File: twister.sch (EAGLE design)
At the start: 30 parts, among them IC1 A3967SLB, U2 ARDUINO_SHIELDNOHOLES

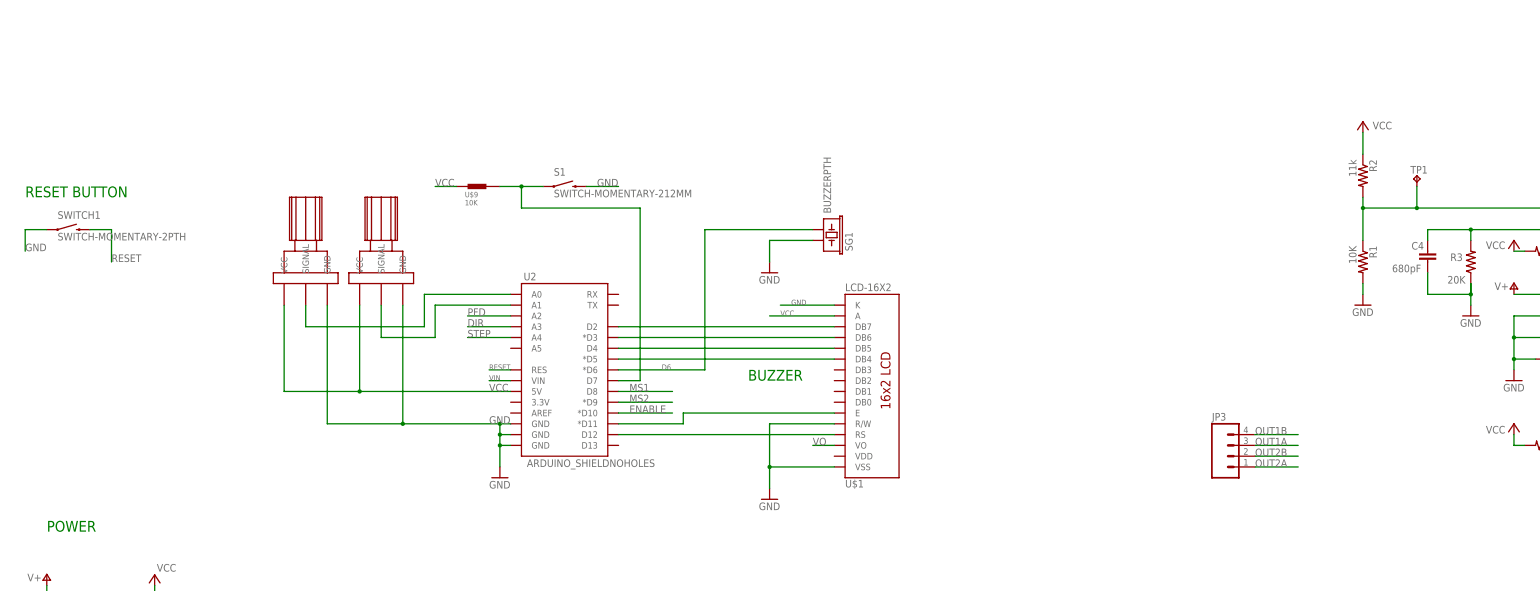
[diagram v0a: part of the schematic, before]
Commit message: Added stepper motor.
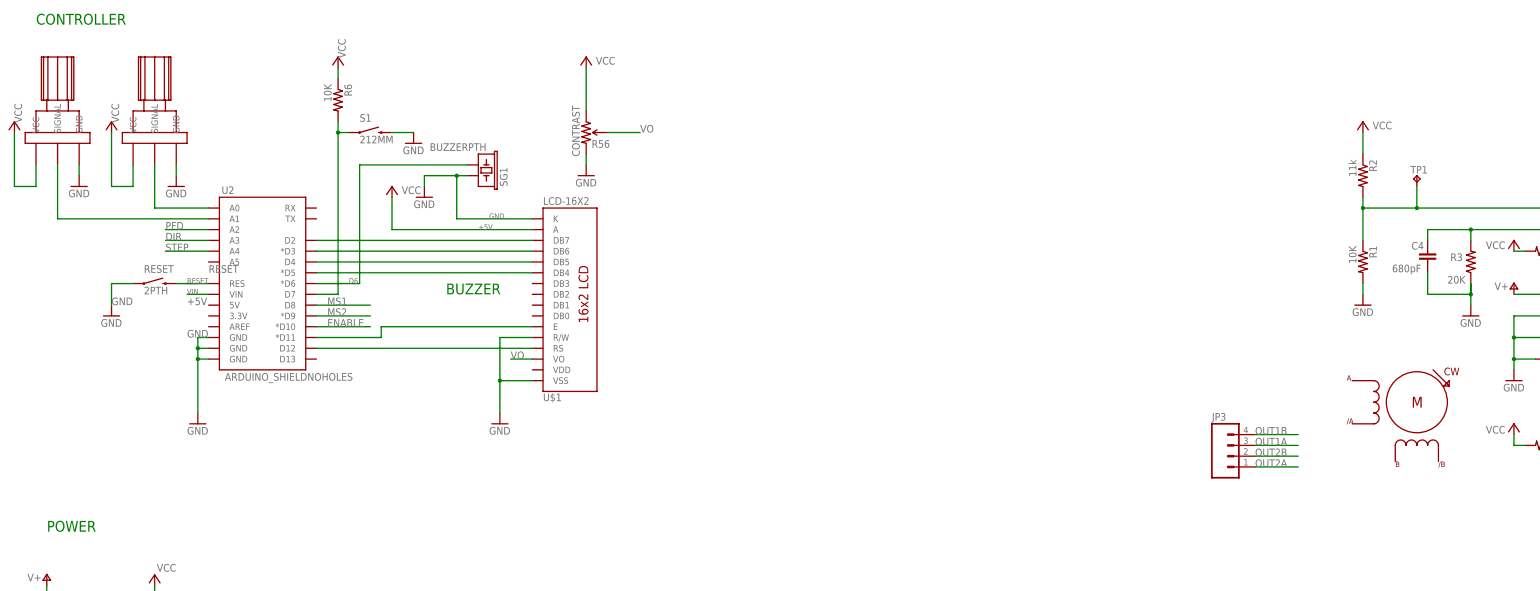
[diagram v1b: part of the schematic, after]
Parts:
- removed SWITCH1: SWITCH-MOMENTARY-2PTH, sparkfun:SWITCH-MOMENTARY-2PTH
- removed U$9: 10K, josh:RESISTOR
- added R56: CONTRAST, sparkfun:TRIMPOT
- added R6: 10K, SparkFun03_30_09:RESISTOR0402
- added RESET: 2PTH, sparkfun:SWITCH-MOMENTARY-2PTH
- added U$2: STEPPER_ST-PM35, twister:STEPPER_ST-PM35
- S1: value SWITCH-MOMENTARY-212MM -> 212MM
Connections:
- removed net VCC: C2.1, IC1.LOGIC_SUPPLY, R10.2, R11.2, R12.2, R14.2, R15.2, R2.1, R9.2, U$1.A, U$10.VCC, U$11.VCC, U$9.P2, U2.5V
- new net +5V: C2.1, IC1.LOGIC_SUPPLY, R10.2, R11.2, R12.2, R14.2, R15.2, R2.1, R56.CCW, R6.1, R9.2, U$1.A, U$10.VCC, U$11.VCC
- net GND: now also R56.CW, RESET.1; no longer SWITCH1.1
- net N$12: now also R6.2; no longer U$9.P1
- net RESET: now also RESET.2; no longer SWITCH1.2
- net VO: now also R56.WIPER
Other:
- note added: "CONTROLLER"
- note removed: "RESET BUTTON"
- note removed: "VO???"
- moved on the sheet: S1, SG1, U$1, U2

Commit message: Everything should be set for final layout.
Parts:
- removed PWR_LED: YELLOW, SparkFun03_30_09:LED0603
- removed R56: CONTRAST, sparkfun:TRIMPOT
- removed R9: 1K, SparkFun03_30_09:RESISTOR0402
- removed S1: 212MM, sparkfun:SWITCH-MOMENTARY-212MM
- removed SG1: BUZZERPTH, sparkfun:BUZZERPTH
- removed U$1: LCD-16X2, sparkfun:LCD-16X2
- removed U$2: STEPPER_ST-PM35, twister:STEPPER_ST-PM35
- added BUZZER: SG1, twister_clean:BUZZERPTH
- added CONTRAST: 10k, twister_clean:TRIMPOT
- added LCD_MODULE: LCD-16X2, twister_clean:LCD-16X2
- added START: 212MM, twister_clean:SWITCH-MOMENTARY-212MM
- added STEPPER: ST-PM35, twister:STEPPER_ST-PM35
- C2: device rcl:C-USC0603 -> twister_clean:C_0805
- C4, C5: device SparkFun03_30_09:CAP0402 -> twister_clean:C_0603
- R1, R10, R11, R12, R13, R14, R15, R17, R2, R3, R4, R6: device SparkFun03_30_09:RESISTOR0402 -> twister_clean:R_0603
- RESET: device sparkfun:SWITCH-MOMENTARY-2PTH -> twister_clean:SWITCH-MOMENTARY-2PTH
- RS1, RS2: device rcl:R-US_R0805 -> twister_clean:R_1206
- U$10, U$11: device josh:LARGE_POT -> twister_clean:LARGE_POT
- U2: device sparkfun:ARDUINO_SHIELDNOHOLES -> twister_clean:ARDUINO_SHIELDNOHOLES
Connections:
- removed net N$17: PWR_LED.A, R9.1
- removed net N$24: U$1.R/W, U$1.VSS
- removed net V+: C1.+
- net +5V: now also CONTRAST.CCW, LCD_MODULE.A, U2.5V; no longer R56.CCW, R9.2, U$1.A
- net D6: now also BUZZER.2; no longer SG1.2
- net GND: now also BUZZER.1, CONTRAST.CW, LCD_MODULE.K, LCD_MODULE.R/W, LCD_MODULE.VSS, START.2; no longer PWR_LED.C, R56.CW, S1.2, SG1.1, U$1.K
- net N$12: now also START.1; no longer S1.1
- net N$4: now also LCD_MODULE.RS; no longer U$1.RS
- net N$5: now also LCD_MODULE.E; no longer U$1.E
- net N$6: now also LCD_MODULE.DB4; no longer U$1.DB4
- net N$7: now also LCD_MODULE.DB5; no longer U$1.DB5
- net N$8: now also LCD_MODULE.DB6; no longer U$1.DB6
- net N$9: now also LCD_MODULE.DB7; no longer U$1.DB7
- net VIN: now also C1.+
- net VO: now also CONTRAST.WIPER, LCD_MODULE.VO; no longer R56.WIPER, U$1.VO
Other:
- note added: "MOTOR OUTPUT"
- note added: "NEED TO MATCH MOTOR TO DRIVER PINOUT TO MAKE SURE DRIVE SEQUENCE IS CORRECT"
- note removed: "BUZZER"
- moved on the sheet: IC1, JP3, TP1

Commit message: Halfway through layout.
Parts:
- removed TP1: TPPAD1-13, testpad:TPPAD1-13
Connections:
- net DIR: now also U2.A1; no longer U2.A3
- net ENABLE: now also U2.D8; no longer U2.*D10
- net MS1: now also U2.*D10; no longer U2.D8
- net N$10: now also U2.A4; no longer U2.A0
- net N$11: now also U2.A5; no longer U2.A1
- net N$14: no longer TP1.TP
- net PFD: now also U2.A3; no longer U2.A2
- net STEP: now also U2.A2; no longer U2.A4
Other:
- note added: "1. NEED TO MATCH MOTOR TO DRIVER PINOUT TO MAKE SURE DRIVE SEQUENCE IS CORRECT 2. PLACE TEST POINTS"
- note removed: "NEED TO MATCH MOTOR TO DRIVER PINOUT TO MAKE SURE DRIVE SEQUENCE IS CORRECT"
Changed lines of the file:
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@@
 <part name="R17" library="twister_clean" deviceset="R" device="_0603" value="???"/>
 <part name="GND10" library="supply1" deviceset="GND" device=""/>
-<part name="TP1" library="testpad" deviceset="TP" device="PAD1-13"/>
 <part name="JP3" library="sparkfun" deviceset="M04" device="1X04_NO_SILK"/>
 <part name="R1" library="twister_clean" deviceset="R" device="_0603" value="10K"/>
@@
 <text x="-12.7" y="147.32" size="2.54" layer="91">CONTROLLER</text>
 <text x="43.18" y="27.94" size="2.54" layer="91">MOTOR OUTPUT</text>
-<text x="99.06" y="15.24" size="1.778" layer="98">NEED TO MATCH MOTOR TO DRIVER PINOUT TO MAKE SURE DRIVE SEQUENCE IS CORRECT</text>
+<text x="147.32" y="139.7" size="1.778" layer="98">1. NEED TO MATCH MOTOR TO DRIVER PINOUT TO MAKE SURE DRIVE SEQUENCE IS CORRECT
+2. PLACE TEST POINTS</text>
 </plain>
 <instances>
@@
 <instance part="R17" gate="R" x="279.4" y="109.22" rot="R180"/>
 <instance part="GND10" gate="1" x="289.56" y="106.68"/>
-<instance part="TP1" gate="G$1" x="167.64" y="116.84"/>
 <instance part="JP3" gate="G$1" x="81.28" y="15.24"/>
 <instance part="R1" gate="R" x="154.94" y="96.52" rot="R270"/>
@@
 <net name="N$10" class="0">
 <segment>
-<wire x1="27.94" y1="104.14" x2="15.24" y2="104.14" width="0.1524" layer="91"/>
-<wire x1="15.24" y1="104.14" x2="15.24" y2="114.3" width="0.1524" layer="91"/>
 <pinref part="U$10" gate="G$1" pin="SIGNAL"/>
-<pinref part="U2" gate="G$1" pin="A0"/>
+<wire x1="15.24" y1="114.3" x2="15.24" y2="93.98" width="0.1524" layer="91"/>
+<pinref part="U2" gate="G$1" pin="A4"/>
+<wire x1="15.24" y1="93.98" x2="27.94" y2="93.98" width="0.1524" layer="91"/>
 </segment>
 </net>
 <net name="N$11" class="0">
 <segment>
-<wire x1="27.94" y1="101.6" x2="-7.62" y2="101.6" width="0.1524" layer="91"/>
-<wire x1="-7.62" y1="101.6" x2="-7.62" y2="114.3" width="0.1524" layer="91"/>
+<wire x1="-7.62" y1="91.44" x2="-7.62" y2="114.3" width="0.1524" layer="91"/>
 <pinref part="U$11" gate="G$1" pin="SIGNAL"/>
-<pinref part="U2" gate="G$1" pin="A1"/>
+<pinref part="U2" gate="G$1" pin="A5"/>
+<wire x1="-7.62" y1="91.44" x2="27.94" y2="91.44" width="0.1524" layer="91"/>
 </segment>
 </net>
 <net name="MS1" class="0">
-<segment>
-<pinref part="U2" gate="G$1" pin="D8"/>
-<wire x1="53.34" y1="81.28" x2="66.04" y2="81.28" width="0.1524" layer="91"/>
-<label x="55.88" y="81.28" size="1.778" layer="95"/>
-</segment>
 <segment>
 <wire x1="203.2" y1="53.34" x2="213.36" y2="53.34" width="0.1524" layer="91"/>
@@
 <pinref part="R14" gate="R" pin="1"/>
 </segment>
+<segment>
+<pinref part="U2" gate="G$1" pin="*D10"/>
+<wire x1="53.34" y1="76.2" x2="66.04" y2="76.2" width="0.1524" layer="91"/>
+<label x="55.88" y="76.2" size="1.778" layer="95"/>
+</segment>
 </net>
 <net name="MS2" class="0">
@@
 <net name="ENABLE" class="0">
 <segment>
-<pinref part="U2" gate="G$1" pin="*D10"/>
-<wire x1="53.34" y1="76.2" x2="66.04" y2="76.2" width="0.1524" layer="91"/>
-<label x="55.88" y="76.2" size="1.778" layer="95"/>
-</segment>
-<segment>
 <wire x1="259.08" y1="63.5" x2="271.78" y2="63.5" width="0.1524" layer="91"/>
 <label x="261.62" y="63.5" size="1.778" layer="95"/>
@@
 <pinref part="R13" gate="R" pin="2"/>
 </segment>
+<segment>
+<pinref part="U2" gate="G$1" pin="D8"/>
+<wire x1="53.34" y1="81.28" x2="66.04" y2="81.28" width="0.1524" layer="91"/>
+<label x="55.88" y="81.28" size="1.778" layer="95"/>
+</segment>
 </net>
 <net name="PFD" class="0">
 <segment>
-<pinref part="U2" gate="G$1" pin="A2"/>
-<wire x1="27.94" y1="99.06" x2="17.78" y2="99.06" width="0.1524" layer="91"/>
-<label x="17.78" y="99.06" size="1.778" layer="95"/>
+<wire x1="27.94" y1="96.52" x2="17.78" y2="96.52" width="0.1524" layer="91"/>
+<label x="17.78" y="96.52" size="1.778" layer="95"/>
+<pinref part="U2" gate="G$1" pin="A3"/>
 </segment>
 <segment>
@@
 <net name="DIR" class="0">
 <segment>
-<pinref part="U2" gate="G$1" pin="A3"/>
-<wire x1="27.94" y1="96.52" x2="17.78" y2="96.52" width="0.1524" layer="91"/>
-<label x="17.78" y="96.52" size="1.778" layer="95"/>
+<wire x1="27.94" y1="101.6" x2="17.78" y2="101.6" width="0.1524" layer="91"/>
+<label x="17.78" y="101.6" size="1.778" layer="95"/>
+<pinref part="U2" gate="G$1" pin="A1"/>
 </segment>
 <segment>
@@
 <net name="STEP" class="0">
 <segment>
-<pinref part="U2" gate="G$1" pin="A4"/>
-<wire x1="27.94" y1="93.98" x2="17.78" y2="93.98" width="0.1524" layer="91"/>
-<label x="17.78" y="93.98" size="1.778" layer="95"/>
+<wire x1="27.94" y1="99.06" x2="17.78" y2="99.06" width="0.1524" layer="91"/>
+<label x="17.78" y="99.06" size="1.778" layer="95"/>
+<pinref part="U2" gate="G$1" pin="A2"/>
 </segment>
 <segment>
@@
 <net name="N$14" class="0">
 <segment>
-<wire x1="154.94" y1="109.22" x2="167.64" y2="109.22" width="0.1524" layer="91"/>
-<wire x1="167.64" y1="109.22" x2="213.36" y2="109.22" width="0.1524" layer="91"/>
-<wire x1="167.64" y1="109.22" x2="167.64" y2="114.3" width="0.1524" layer="91"/>
-<junction x="167.64" y="109.22"/>
+<wire x1="154.94" y1="109.22" x2="213.36" y2="109.22" width="0.1524" layer="91"/>
 <pinref part="IC1" gate="G$1" pin="REF"/>
-<pinref part="TP1" gate="G$1" pin="TP"/>
 <pinref part="R1" gate="R" pin="1"/>
 <pinref part="R2" gate="R" pin="2"/>

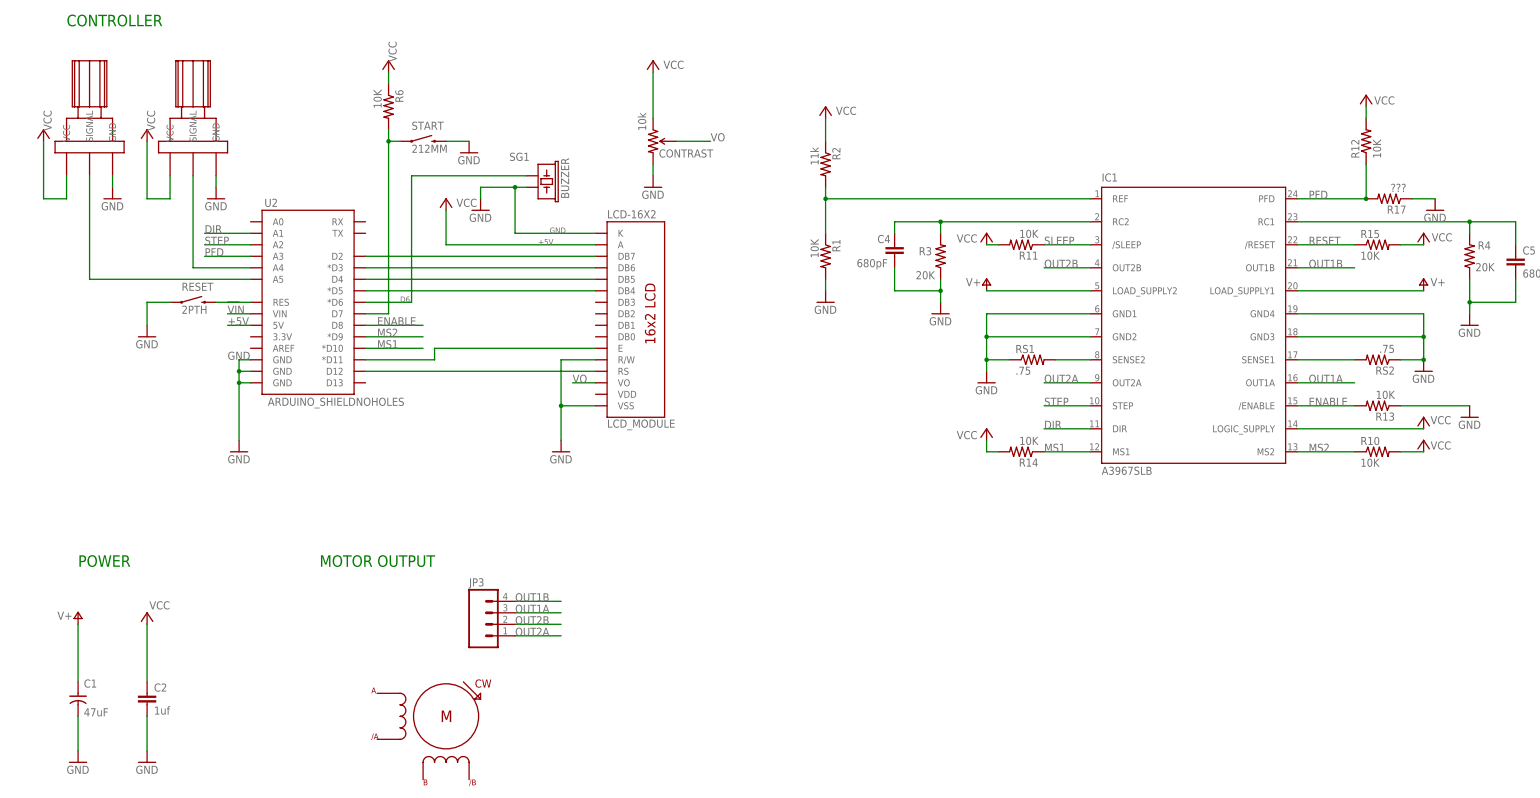
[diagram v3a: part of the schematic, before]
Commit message: Just about finished. Need to clean up aux materials so they actually match the pcb.
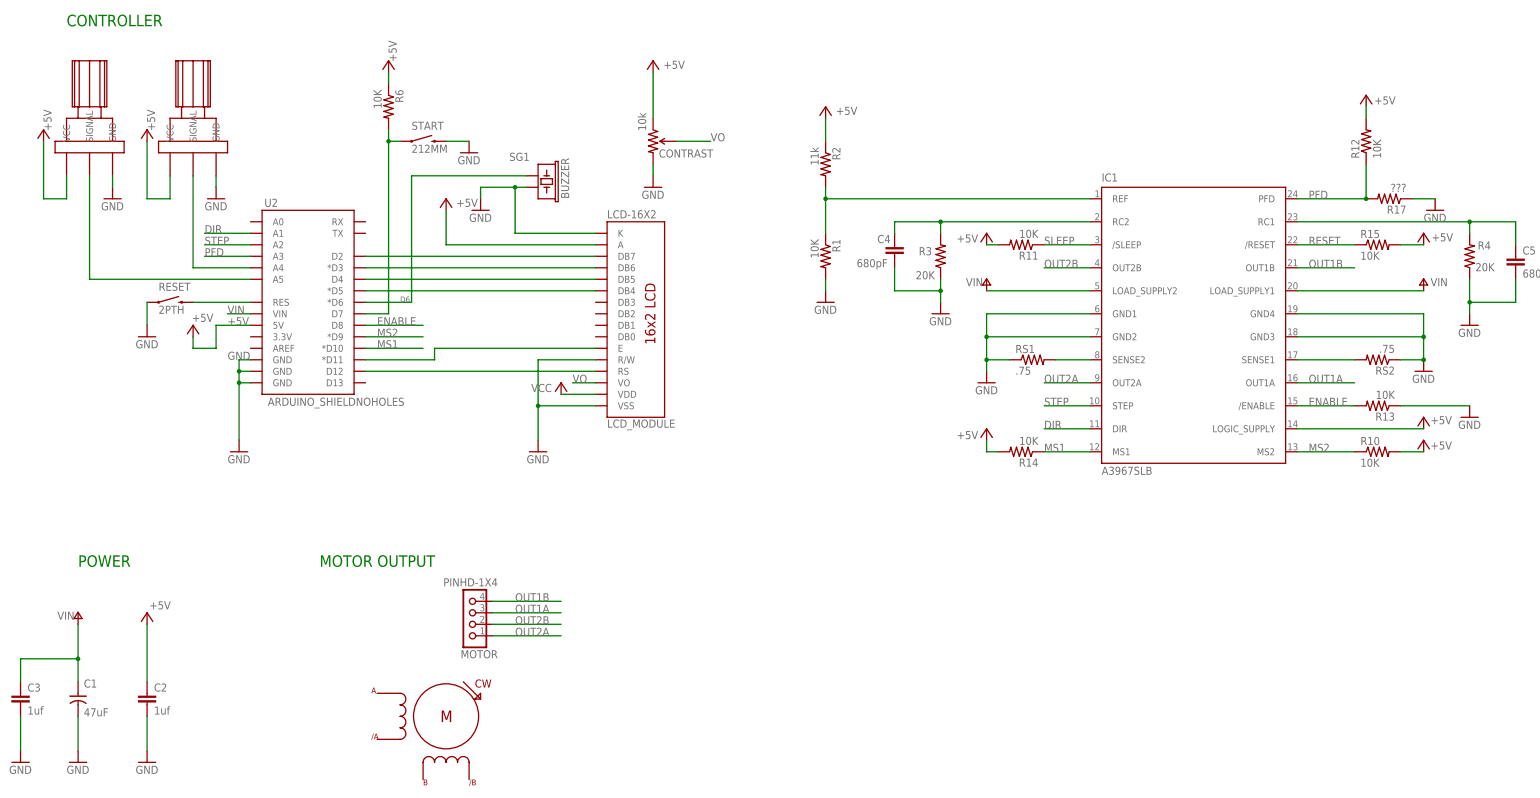
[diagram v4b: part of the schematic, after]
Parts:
- removed JP3: (no value), sparkfun:M041X04_NO_SILK
- added C3: 1uf, twister_clean:C_0805
- added MOTOR: PINHD-1X4, twister_clean:PINHD-1X4
- IC1: device Allegro:A3967SLB -> twister_clean:A3967SLB
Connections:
- net +5V: now also LCD_MODULE.VDD
- net GND: now also C3.2
- net OUT1A: now also MOTOR.3; no longer JP3.3
- net OUT1B: now also MOTOR.4; no longer JP3.4
- net OUT2A: now also MOTOR.1; no longer JP3.1
- net OUT2B: now also MOTOR.2; no longer JP3.2
- net VIN: now also C3.1
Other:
- moved on the sheet: RESET

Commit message: Finished rev 1.0 and sent to fab.
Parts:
- removed R15: 10K, twister_clean:R_0603
- removed R17: ???, twister_clean:R_0603
- removed U$10, U$11: LARGE_POT, twister_clean:LARGE_POT
- added R5, R7, R8, R9: 10K, twister_clean:R_0603
- C1: value 47uF -> 1uF; device cyclops:C-POL_0807 -> twister_clean:C_0805
- C2: value 1uf -> 47uF; device twister_clean:C_0805 -> cyclops:C-POL_0807
- C3: value 1uf -> 1uF
- R1: value 10K -> R12-0; device twister_clean:R_0603 -> twister_clean:LARGE_POT
- R13: value 10K -> ???
- R14, R6: value 10K -> 20K
- R2: value 11k -> R12-0; device twister_clean:R_0603 -> twister_clean:LARGE_POT
- R3: value 20K -> 10K
- R4: value 20K -> 11K
- renumbered U2 to U1
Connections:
- net +5V: now also C3.1, R1.VCC, R2.VCC, R3.1, R4.1, R7.2, R8.2, R9.2; no longer C2.1, R11.2, R14.2, R15.2, R2.1, R6.1, U$10.VCC, U$11.VCC
- net ENABLE: now also R11.2; no longer R13.2
- net GND: now also C1.2, C2.-, R1.GND, R11.1, R14.1, R2.GND, R5.2, R6.1; no longer C1.-, C2.2, R1.2, R17.1, R3.1, R4.1, U$10.GND, U$11.GND
- net MS1: now also R8.1; no longer R14.1
- net MS2: now also R12.1; no longer R10.1
- net N$10: now also R2.SIGNAL; no longer U$10.SIGNAL
- net N$11: now also R1.SIGNAL; no longer U$11.SIGNAL
- net N$12: now also R3.2; no longer R6.2
- net N$13: now also R14.2; no longer R4.2
- net N$14: now also R4.2, R5.1; no longer R1.1, R2.2
- net N$2: now also R6.2; no longer R3.2
- net PFD: now also R13.2, R9.1; no longer R12.1, R17.2
- net RESET: now also R10.1; no longer R15.1
- net SLEEP: now also R7.1; no longer R11.1
- net VIN: now also C1.1, C2.+; no longer C1.+, C3.1
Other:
- note added: "Change R9 and add in"
- note added: "R13 to create any voltage"
- note removed: "1. NEED TO MATCH MOTOR TO DRIVER PINOUT TO MAKE SURE DRIVE SEQUENCE IS CORRECT 2. PLACE TEST POINTS"
- note removed: "Change R12 and add in"
- note removed: "R17 to create any voltage"
- moved on the sheet: C1, C2, C3, R10, R11, R12, R13, R14, R3, R4, R6
